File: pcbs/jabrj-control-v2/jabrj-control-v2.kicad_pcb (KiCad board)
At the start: 6 copper layers, 70 x 80 mm, 300 parts, among them J1001 FH12-22S-0.5SH, J1002 FH12-22S-0.5SH, J301 43045-0201, J401 MDT420E0X001, J701 FFC3A20-05-G, J702 JST-SH-4-Vertical, J801 MSPE-J2L0-x00, J901 48406-0003, J902 ARJM11D7-502-AB-EW2, J903 TYPE-C-31-M-12, Q401 DMN21D2UFB-7B, Q402 DMN21D2UFB-7B, Q403 DMN21D2UFB-7B, Q701 DMN21D2UFB-7B, SW701 TS20-42-25-WT-160-SMT-TR, U301 SYA75603A, U302 TVS3301DRBR, U303 PCI11010C, U304 TPS26600RHFR, U305 AT24C64D-MAHM-E, U401 AZV3001FZ4-7, U402 TPS259472ARPWR, U403 MAX20008AFOC/VY+T, U501 TPS7B8133QDRVRQ1, U502 TPS2116DRL, U601 TPS22991CNRAAR, U602 TPS62827DMQR, U603 TPS62825DMQR, U701 PESD4USB3BTTS-QX, U702 NX3DV221GM, U801 LAN8870, U901 PESD4USB3BTTS-QX, U902 PESD4USB3BTTS-QX, U903 PESD4USB3BTTS-QX, U904 PESD4USB3BTTS-QX, U905 PESD4USB3BTTS-QX, U906 AP22653FDZ-7, U907 PESD4USB3BTTS-QX, Y301 XRCGB25M000F3A16R0, Y401 ASEK-32.768KHZ-LRT, Y801 XRCGB25M000F3A16R0

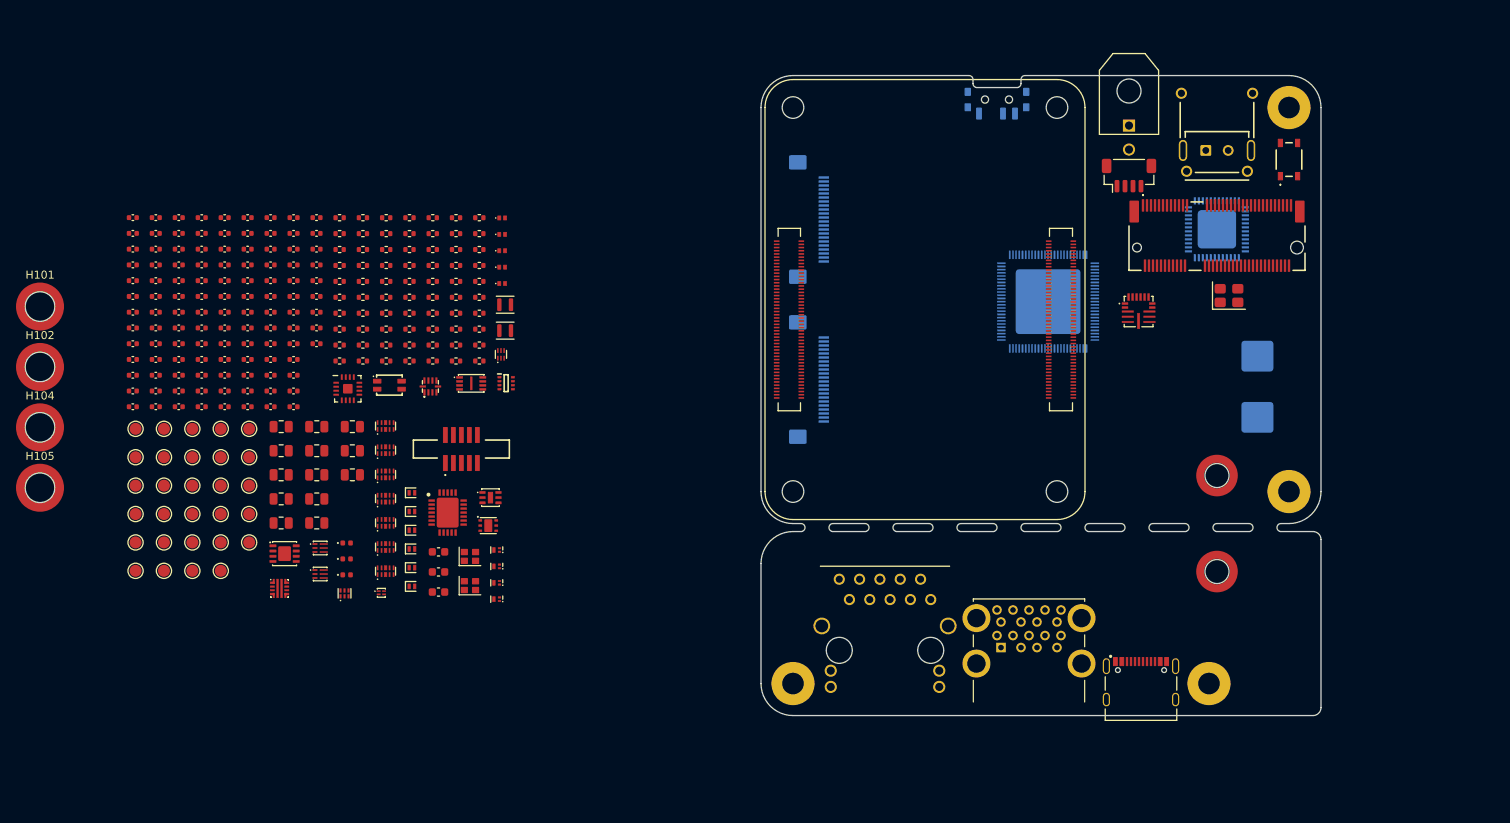
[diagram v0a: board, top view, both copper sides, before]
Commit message: Fixed 5V buck inductor value
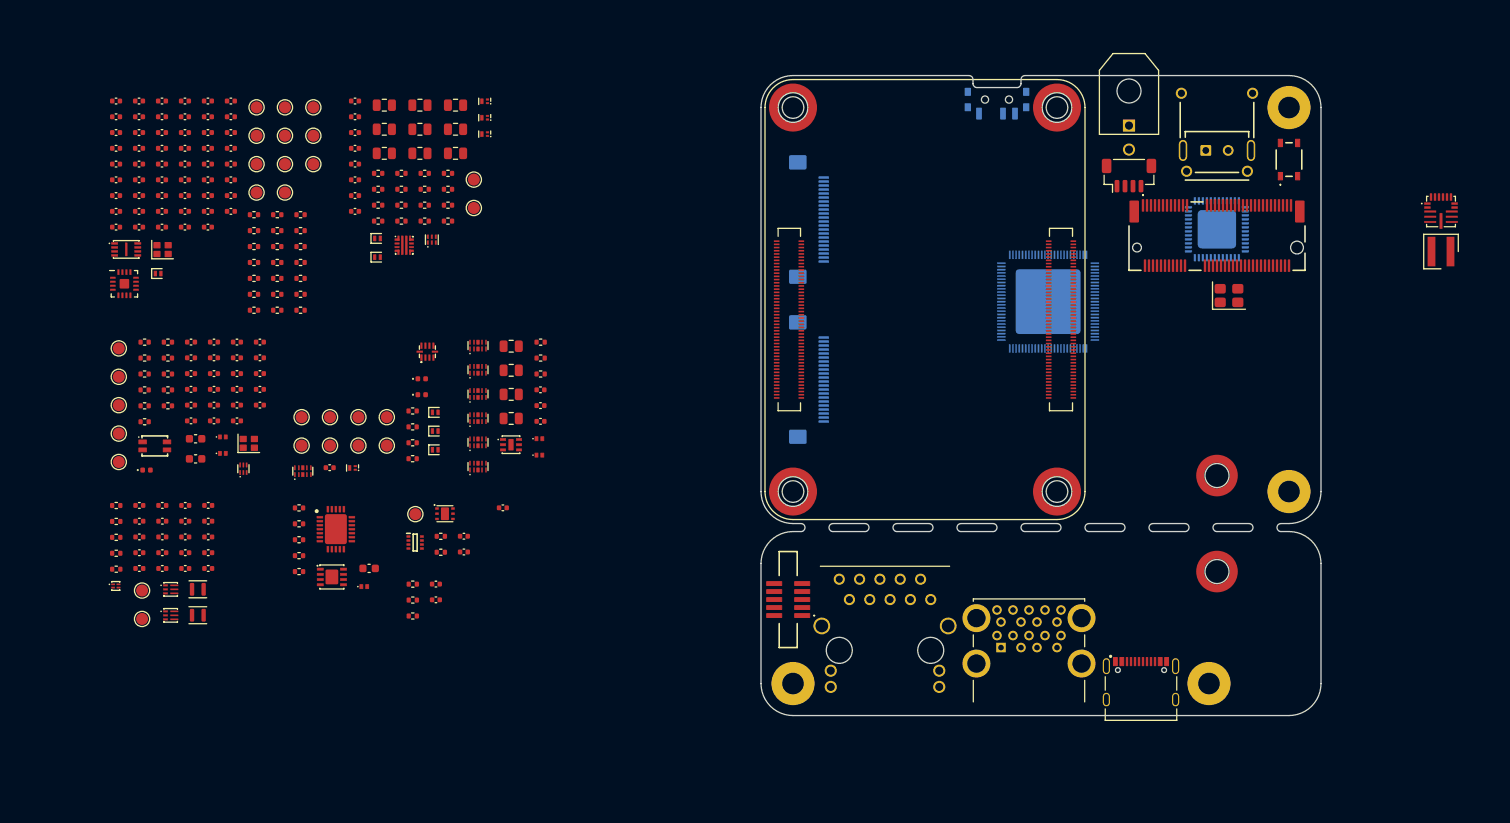
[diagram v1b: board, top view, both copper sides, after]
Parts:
- removed C302, C303, C304, C305, C306, C307, C312, C313, C314, C319, C320, C321, C326, C327, C328, C330, C331, C335, C337, C338, C339, C341, C343, C345, C347, C352: 1n, project_footprints:C_0402
- removed C308, C309, C322, C323, C332, C333, C336, C340, C342, C344, C346, C348, C349, C351, C810, C811, C812, C813, C814, C815, C818, C819, C820: 100n, project_footprints:C_0402
- removed C310, C311, C324, C325, C334, C808, C817: 1u, project_footprints:C_0402
- removed C315, C316, C317, C318: 220n, project_footprints:C_0402
- removed C329, C824, C825: 100n, project_footprints:C_0603
- removed C350, C809, C816, C823, C906, C907: 4u7, project_footprints:C_0402
- removed C353, C354, C821, C822: 10p, project_footprints:C_0402
- removed C418, C903, C904, C905: 22u, project_footprints:C_0805
- removed D302, D803, D804: SZESD7241N2T5G, project_footprints:SZESD7462N2T5G
- removed D901, D902: SZESD8472MUT5G, project_footprints:SZESD7462N2T5G
- removed FL801: ACT1210G-800-2P-TL10, project_footprints:ACT1210G
- removed L401: 784325078, project_footprints:784325078
- removed R306, R315, R319, R325, R326, R810: 1k, project_footprints:R_0402
- removed R307, R312, R322: 100k, project_footprints:R_0402
- removed R308: 120k, project_footprints:R_0402
- removed R309, R311, R314, R316, R317, R320, R321, R324, R804, R805, R807, R808, R809, R811: 10k, project_footprints:R_0402
- removed R310: 4k7, project_footprints:R_0402
- removed R313: 2k2, project_footprints:R_0402
- removed R318: 22k, project_footprints:R_0402
- removed R323: 200R, project_footprints:R_0402
- removed R806: 12k1, project_footprints:R_0402
- removed TP301, TP302, TP303, TP304, TP305, TP306, TP307, TP308, TP309, TP310, TP311, TP801, TP802, TP803, TP804, TP805: 1.5mm, project_footprints:TestPoint_Pad_D1.5mm
- removed U304: TPS26600RHFR, project_footprints:QFN50P400X500X100-25N-D
- removed U305: AT24C64D-MAHM-E, project_footprints:SON50P300X200X60-9N
- removed U901, U902, U903, U904, U905, U907: PESD4USB3BTTS-QX, project_footprints:PESD4USB3BTTSQX
- removed U906: AP22653FDZ-7, project_footprints:SON65P200X200X80-7N-D
- removed Y301, Y801: XRCGB25M000F3A16R0, project_footprints:XRCGB25M000F3A16R0
- added C1003: 1n, project_footprints:C_0402, F.Cu at (48.4, 70.1)
- added C1004: 1n, project_footprints:C_0402, F.Cu at (48.4, 72.1)
- added C1005: 1n, project_footprints:C_0402, F.Cu at (48.4, 74.1)
- added C1006: 1n, project_footprints:C_0402, F.Cu at (48.4, 76.0)
- added C1007: 1n, project_footprints:C_0402, F.Cu at (48.4, 78.0)
- added C1008: 100n, project_footprints:C_0402, F.Cu at (48.4, 80.0)
- added C1009: 100n, project_footprints:C_0402, F.Cu at (48.4, 81.9)
- added C1010: 1u, project_footprints:C_0402, F.Cu at (51.3, 66.2)
- added C1011: 1u, project_footprints:C_0402, F.Cu at (51.3, 68.2)
- added C1012: 1n, project_footprints:C_0402, F.Cu at (51.3, 70.1)
- added C1013: 1n, project_footprints:C_0402, F.Cu at (51.3, 72.1)
- added C1014: 1n, project_footprints:C_0402, F.Cu at (51.3, 74.1)
- added C1015: 220n, project_footprints:C_0402, F.Cu at (51.3, 76.0)
- added C1016: 220n, project_footprints:C_0402, F.Cu at (51.3, 78.0)
- added C1017: 220n, project_footprints:C_0402, F.Cu at (51.3, 80.0)
- added C1018: 220n, project_footprints:C_0402, F.Cu at (51.3, 81.9)
- added C1019: 1n, project_footprints:C_0402, F.Cu at (54.1, 66.2)
- added C1020: 1n, project_footprints:C_0402, F.Cu at (54.1, 68.2)
- added C1021: 1n, project_footprints:C_0402, F.Cu at (54.1, 70.1)
- added C1022: 100n, project_footprints:C_0402, F.Cu at (54.1, 72.1)
- added C1023: 100n, project_footprints:C_0402, F.Cu at (54.1, 74.1)
- added C1024: 1u, project_footprints:C_0402, F.Cu at (54.1, 76.0)
- added C1025: 1u, project_footprints:C_0402, F.Cu at (54.1, 78.0)
- added C1026: 1n, project_footprints:C_0402, F.Cu at (54.1, 80.0)
- added C1027: 1n, project_footprints:C_0402, F.Cu at (54.1, 81.9)
- added C1028: 1n, project_footprints:C_0402, F.Cu at (57.0, 66.2)
- added C1029: 1n, project_footprints:C_0402, F.Cu at (57.0, 68.2)
- added C1030: 1n, project_footprints:C_0402, F.Cu at (57.0, 70.1)
- added C1031: 100n, project_footprints:C_0402, F.Cu at (57.0, 72.1)
- added C1032: 100n, project_footprints:C_0402, F.Cu at (57.0, 74.1)
- added C1033: 1u, project_footprints:C_0402, F.Cu at (57.0, 76.0)
- added C1034: 1n, project_footprints:C_0402, F.Cu at (57.0, 78.0)
- added C1035: 100n, project_footprints:C_0402, F.Cu at (57.0, 80.0)
- added C1036: 1n, project_footprints:C_0402, F.Cu at (57.0, 81.9)
- added C1037: 1n, project_footprints:C_0402, F.Cu at (59.9, 66.2)
- added C1038: 1n, project_footprints:C_0402, F.Cu at (59.9, 68.2)
- added C1039: 100n, project_footprints:C_0402, F.Cu at (59.9, 70.1)
- added C1040: 1n, project_footprints:C_0402, F.Cu at (59.9, 72.1)
- added C1041: 100n, project_footprints:C_0402, F.Cu at (59.9, 74.1)
- added C1042: 1n, project_footprints:C_0402, F.Cu at (59.9, 76.0)
- added C1043: 100n, project_footprints:C_0402, F.Cu at (59.9, 78.0)
- added C1044: 1n, project_footprints:C_0402, F.Cu at (59.9, 80.0)
- added C1045: 100n, project_footprints:C_0402, F.Cu at (59.9, 81.9)
- added C1046: 1n, project_footprints:C_0402, F.Cu at (62.7, 66.2)
- added C1047: 100n, project_footprints:C_0402, F.Cu at (62.7, 68.2)
- added C1048: 100n, project_footprints:C_0402, F.Cu at (62.7, 70.1)
- added C1049: 4u7, project_footprints:C_0402, F.Cu at (62.7, 72.1)
- added C1050: 100n, project_footprints:C_0402, F.Cu at (62.7, 74.1)
- added C1051: 1n, project_footprints:C_0402, F.Cu at (62.7, 76.0)
- added C1052: 10p, project_footprints:C_0402, F.Cu at (62.7, 78.0)
- added C1053: 10p, project_footprints:C_0402, F.Cu at (62.7, 80.0)
- added C1101: 100n, project_footprints:C_0402, F.Cu at (57.8, 96.3)
- added C1102: 100n, project_footprints:C_0402, F.Cu at (57.8, 98.3)
- added C1103: 4u7, project_footprints:C_0402, F.Cu at (57.8, 100.3)
- added C1104: 100n, project_footprints:C_0402, F.Cu at (57.8, 102.2)
- added C1105: 100n, project_footprints:C_0402, F.Cu at (57.8, 104.2)
- added C1106: 100n, project_footprints:C_0402, F.Cu at (57.8, 106.2)
- added C1107: 1u, project_footprints:C_0402, F.Cu at (60.6, 96.3)
- added C1108: 1u, project_footprints:C_0402, F.Cu at (60.6, 98.3)
- added C1109: 4u7, project_footprints:C_0402, F.Cu at (60.6, 100.3)
- added C1110: 100n, project_footprints:C_0402, F.Cu at (60.6, 102.2)
- added C1111: 100n, project_footprints:C_0402, F.Cu at (60.6, 104.2)
- added C1112: 100n, project_footprints:C_0402, F.Cu at (60.6, 106.2)
- added C1113: 100n, project_footprints:C_0402, F.Cu at (63.5, 96.3)
- added C1114: 100n, project_footprints:C_0402, F.Cu at (63.5, 98.3)
- added C1115: 100n, project_footprints:C_0402, F.Cu at (63.5, 100.3)
- added C1116: 4u7, project_footprints:C_0402, F.Cu at (63.5, 102.2)
- added C1117: 1u, project_footprints:C_0402, F.Cu at (63.5, 104.2)
- added C1118: 100n, project_footprints:C_0402, F.Cu at (63.5, 106.2)
- added C1119: 100n, project_footprints:C_0402, F.Cu at (66.4, 96.3)
- added C1120: 100n, project_footprints:C_0402, F.Cu at (66.4, 98.3)
- added C1121: 10p, project_footprints:C_0402, F.Cu at (66.4, 100.3)
- added C1122: 10p, project_footprints:C_0402, F.Cu at (66.4, 102.2)
- added C1123: 4u7, project_footprints:C_0402, F.Cu at (66.4, 104.2)
- added C1124: 100n, project_footprints:C_0603, F.Cu at (58.3, 108.4)
- added C1125: 100n, project_footprints:C_0603, F.Cu at (58.3, 110.9)
- added C1201: 100n, project_footprints:C_0402, F.Cu at (96.7, 117.0)
- added D1001: PMEG4002EL-QYL, project_footprints:PMEG4002EL-QYL, F.Cu at (53.6, 87.8)
- added D1101: GREEN, project_footprints:LED_0402, F.Cu at (52.2, 112.3)
- added D1102: 824012823, project_footprints:824012823, F.Cu at (64.3, 112.2)
- added D1103: SZESD7241N2T5G, project_footprints:SZESD7462N2T5G, F.Cu at (61.7, 108.2)
- added D1104: SZESD7241N2T5G, project_footprints:SZESD7462N2T5G, F.Cu at (61.7, 110.2)
- added FL1101: ACT1210G-800-2P-TL10, project_footprints:ACT1210G, F.Cu at (53.2, 109.3)
- added L402: 7443844020010, project_footprints:L_Wurth_WE-MXGI-4020, F.Cu at (214.0, 85.0)
- added R1004: 1k, project_footprints:R_0402, F.Cu at (65.6, 86.4)
- added R1005: 10k, project_footprints:R_0402, F.Cu at (65.6, 88.4)
- added R1006: 1k, project_footprints:R_0402, F.Cu at (65.6, 90.3)
- added R1007: 100k, project_footprints:R_0402, F.Cu at (65.6, 92.3)
- added R1008: 10k, project_footprints:R_0402, F.Cu at (68.5, 80.4)
- added R1009: 100k, project_footprints:R_0402, F.Cu at (68.5, 82.4)
- added R1010: 2k2, project_footprints:R_0402, F.Cu at (68.5, 84.4)
- added R1011: 1k, project_footprints:R_0402, F.Cu at (68.5, 86.4)
- added R1012: 10k, project_footprints:R_0402, F.Cu at (68.5, 88.4)
- added R1013: 10k, project_footprints:R_0402, F.Cu at (68.5, 90.3)
- added R1014: 1k, project_footprints:R_0402, F.Cu at (68.5, 92.3)
- added R1015: 10k, project_footprints:R_0402, F.Cu at (71.4, 80.4)
- added R1016: 10k, project_footprints:R_0402, F.Cu at (71.4, 82.4)
- added R1017: 100k, project_footprints:R_0402, F.Cu at (71.4, 84.4)
- added R1018: 200R, project_footprints:R_0402, F.Cu at (71.4, 86.4)
- added R1019: 10k, project_footprints:R_0402, F.Cu at (71.4, 88.4)
- added R1020: 1k, project_footprints:R_0402, F.Cu at (71.4, 90.3)
- added R1021: 1k, project_footprints:R_0402, F.Cu at (71.4, 92.3)
- added R1101: 10k, project_footprints:R_0402, F.Cu at (52.0, 96.3)
- added R1102: 10k, project_footprints:R_0402, F.Cu at (52.0, 98.3)
- added R1103: 10k, project_footprints:R_0402, F.Cu at (52.0, 100.3)
- added R1104: 10k, project_footprints:R_0402, F.Cu at (52.0, 102.3)
- added R1105: 10k, project_footprints:R_0402, F.Cu at (52.0, 104.3)
- added R1106: 12k1, project_footprints:R_0402, F.Cu at (52.0, 106.3)
- added R1107: 10k, project_footprints:R_0402, F.Cu at (54.9, 96.3)
- added R1108: 10k, project_footprints:R_0402, F.Cu at (54.9, 98.3)
- added R1109: 10k, project_footprints:R_0402, F.Cu at (54.9, 100.3)
- added R1110: 1k, project_footprints:R_0402, F.Cu at (54.9, 102.3)
- added R1111: 10k, project_footprints:R_0402, F.Cu at (54.9, 104.3)
- added TP1001: 1.5mm, project_footprints:TestPoint_Pad_D1.5mm, F.Cu at (65.9, 67.0)
- added TP1002: 1.5mm, project_footprints:TestPoint_Pad_D1.5mm, F.Cu at (65.9, 70.5)
- added TP1003: 1.5mm, project_footprints:TestPoint_Pad_D1.5mm, F.Cu at (65.9, 74.1)
- added TP1004: 1.5mm, project_footprints:TestPoint_Pad_D1.5mm, F.Cu at (65.9, 77.6)
- added TP1005: 1.5mm, project_footprints:TestPoint_Pad_D1.5mm, F.Cu at (69.5, 67.0)
- added TP1006: 1.5mm, project_footprints:TestPoint_Pad_D1.5mm, F.Cu at (69.5, 70.5)
- added TP1007: 1.5mm, project_footprints:TestPoint_Pad_D1.5mm, F.Cu at (69.5, 74.1)
- added TP1008: 1.5mm, project_footprints:TestPoint_Pad_D1.5mm, F.Cu at (69.5, 77.6)
- added TP1009: 1.5mm, project_footprints:TestPoint_Pad_D1.5mm, F.Cu at (73.0, 67.0)
- added TP1010: 1.5mm, project_footprints:TestPoint_Pad_D1.5mm, F.Cu at (73.0, 70.5)
- added TP1011: 1.5mm, project_footprints:TestPoint_Pad_D1.5mm, F.Cu at (73.0, 74.1)
- added TP1101: 1.5mm, project_footprints:TestPoint_Pad_D1.5mm, F.Cu at (48.7, 97.1)
- added TP1102: 1.5mm, project_footprints:TestPoint_Pad_D1.5mm, F.Cu at (48.7, 100.7)
- added TP1103: 1.5mm, project_footprints:TestPoint_Pad_D1.5mm, F.Cu at (48.7, 104.2)
- added TP1104: 1.5mm, project_footprints:TestPoint_Pad_D1.5mm, F.Cu at (48.7, 107.8)
- added TP1105: 1.5mm, project_footprints:TestPoint_Pad_D1.5mm, F.Cu at (48.7, 111.3)
- added U1001: SYA75603A, project_footprints:SYA7560x, F.Cu at (49.4, 89.0)
- added U1003: AT24C64D-MAHM-E, project_footprints:SON50P300X200X60-9N, F.Cu at (49.6, 84.7)
- added U801: PESD4USB3BTTS-QX, project_footprints:PESD4USB3BTTSQX, F.Cu at (93.6, 96.8)
- added U802: PESD4USB3BTTS-QX, project_footprints:PESD4USB3BTTSQX, F.Cu at (93.6, 99.8)
- added U803: PESD4USB3BTTS-QX, project_footprints:PESD4USB3BTTSQX, F.Cu at (93.6, 102.8)
- added U804: PESD4USB3BTTS-QX, project_footprints:PESD4USB3BTTSQX, F.Cu at (93.6, 105.8)
- added U805: PESD4USB3BTTS-QX, project_footprints:PESD4USB3BTTSQX, F.Cu at (93.6, 108.9)
- added U806: AP22653FDZ-7, project_footprints:SON65P200X200X80-7N-D, F.Cu at (97.8, 109.1)
- added U807: PESD4USB3BTTS-QX, project_footprints:PESD4USB3BTTSQX, F.Cu at (93.6, 111.9)
- added Y1001: XRCGB25M000F3A16R0, project_footprints:XRCGB25M000F3A16R0, F.Cu at (54.2, 84.8)
- added Y1101: XRCGB25M000F3A16R0, project_footprints:XRCGB25M000F3A16R0, F.Cu at (65.0, 109.0)
- C1001, C1002: value 4u7 -> 1n
- C301: value 1n -> 100n; footprint project_footprints:C_0402 -> project_footprints:C_0603
- C414, C802, C804, C805: value 100n -> 22u; footprint project_footprints:C_0402 -> project_footprints:C_0805
- C803: value 4u7 -> 22u; footprint project_footprints:C_0402 -> project_footprints:C_0805
- C806, C901: value 100n -> 4u7
- C807: value 1u -> 4u7
- C902: value 22u -> 4u7; footprint project_footprints:C_0805 -> project_footprints:C_0402
- D301: value PMEG4002EL-QYL -> SZESD7241N2T5G; footprint project_footprints:PMEG4002EL-QYL -> project_footprints:SZESD7462N2T5G
- D801: value GREEN -> SZESD8472MUT5G; footprint project_footprints:LED_0402 -> project_footprints:SZESD7462N2T5G
- D802: value 824012823 -> SZESD8472MUT5G; footprint project_footprints:824012823 -> project_footprints:SZESD7462N2T5G
- R1001, R1002, R1003: value 2k2 -> 10k
- R301: value 10k -> 120k
- R303: value 10k -> 4k7
- R304: value 1k -> 10k
- R305: value 10k -> 22k
- R801, R802: value 10k -> 470R
- R803: value 10k -> 12k1
- R901, R902: value 470R -> 2k2
- R903: value 12k1 -> 2k2
- U301: value SYA75603A -> TVS3301DRBR; footprint project_footprints:SYA7560x -> project_footprints:SON65P300X300X100-9N-D
- U302: value TVS3301DRBR -> TPS26600RHFR; footprint project_footprints:SON65P300X300X100-9N-D -> project_footprints:QFN50P400X500X100-25N-D
- moved H104 133.3 mm to (166.0, 67.0)
- moved H105 127.1 mm to (166.0, 115.0)
- moved H101 97.4 mm to (133.0, 67.0)
- moved H102 95.4 mm to (133.0, 115.0)
- moved Q401 58.2 mm to (94.5, 66.2)
- moved Q403 58.2 mm to (94.5, 70.3)
- moved Q402 58.2 mm to (94.5, 68.3)
- moved R602 56.7 mm to (48.4, 118.7)
- moved R603 56.7 mm to (48.4, 120.7)
- moved R604 56.7 mm to (48.4, 122.7)
- moved R605 56.7 mm to (48.4, 124.7)
- moved C415 55.0 mm to (90.8, 66.7)
- moved C402 53.8 mm to (81.9, 66.7)
- moved L601 52.4 mm to (58.6, 127.2)
- moved L602 52.4 mm to (58.6, 130.5)
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- renumbered H401 to H1201, H402 to H1202, J801 to J1101, J401 to J1201, J901 to J801, J902 to J802, J903 to J803, J1001 to J901, J1002 to J902, U303 to U1002, U801 to U1101, Y401 to Y1201
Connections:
- C1001 pad 1: +3V3 -> +1V1
- C1002 pad 1: +3V3 -> +3V3_PCIE
- C301 pad 1: +1V1 -> GND
- C301 pad 2: GND -> /Power/Power In/VIN_RAW
- C414 pad 1: +3V3_PCIE -> +5V
- C801 pad 1: +3V3_PCIE -> /CM5IO/CT
- C802 pad 1: +3V3_PCIE -> /CM5IO/VBUS_OUT
- C803 pad 1: +3V3_PCIE -> /CM5IO/VBUS_OUT
- C804 pad 1: +3V3_PCIE -> /CM5IO/VBUS_OUT
- C805 pad 1: +3V3_PCIE -> /CM5IO/VBUS_OUT
- C806 pad 1: +3V3_AON -> +5V
- C807 pad 1: +3V3_PCIE -> +5V
- C901 pad 1: /CM5IO/CT -> +3V3
- C902 pad 1: /CM5IO/VBUS_OUT -> +3V3
- D301 pad 1: /PCIe Switch/~{PORT1_CLKREQ} -> GND
- D301 pad 2: /PCIe Switch/~{OE0} -> /Power/Power In/VIN_RAW
- D801 pad 1: /1000BASE-T1 PHY/LINK_LED -> GND
- D801 pad 2: +1V8_PCIE -> /CM5IO/VBUS_OUT
- D802 pad 1: /1000BASE-T1 PHY/TRXN -> VBUS
- D802 pad 2: /1000BASE-T1 PHY/TRXP -> GND
- R1001 pad 1: /MIPI Connectors/~{MIPI1_RST} -> +3V3_PCIE
- R1001 pad 2: +3V3 -> /PCIe Switch/~{PORT1_CLKREQ}
- R1002 pad 1: /CM5/MIPI1.SCL -> +1V8_PCIE
- R1002 pad 2: +3V3 -> /PCIe Switch/~{OE0}
- R1003 pad 1: /CM5/MIPI1.SDA -> +3V3_PCIE
- R1003 pad 2: +3V3 -> /M.2 E-Key/M2_I2C.~{INT}
- R301 pad 1: +3V3_PCIE -> /Power/Power In/VIN_RAW
- R301 pad 2: /PCIe Switch/~{PORT1_CLKREQ} -> /Power/Power In/UVLO
- R302 pad 1: +1V8_PCIE -> /Power/Power In/UVLO
- R302 pad 2: /PCIe Switch/~{OE0} -> /Power/Power In/OVP
- R303 pad 1: +3V3_PCIE -> /Power/Power In/OVP
- R303 pad 2: /M.2 E-Key/M2_I2C.~{INT} -> /Power/Power In/RTN
- R304 pad 1: +3V3_PCIE -> /Power/Power In/RTN
- R304 pad 2: /M.2 E-Key/M2_I2C.SCL -> /Power/Power In/ILIM
- R305 pad 1: /PCIe Switch/VAUX_DET -> /Power/Power In/RTN
- R305 pad 2: GND -> /Power/Power In/ILIM
- R801 pad 1: +1V8_PCIE -> /CM5IO/LEDG
- R801 pad 2: /1000BASE-T1 PHY/RX_D0 -> /CM5/ETH_LED2
- R802 pad 1: /1000BASE-T1 PHY/RX_D1 -> /CM5IO/LEDY
- R802 pad 2: GND -> /CM5/ETH_LED3
- R803 pad 1: /1000BASE-T1 PHY/RX_D2 -> /CM5IO/ILIM
- R901 pad 1: /CM5IO/LEDG -> /MIPI Connectors/~{MIPI1_RST}
- R901 pad 2: /CM5/ETH_LED2 -> +3V3
- R902 pad 1: /CM5IO/LEDY -> /CM5/MIPI1.SCL
- R902 pad 2: /CM5/ETH_LED3 -> +3V3
- R903 pad 1: /CM5IO/ILIM -> /CM5/MIPI1.SDA
- R903 pad 2: GND -> +3V3
- U301 pad 1: /CM5/CLK_P -> /Power/Power In/VIN_RAW
- U301 pad 2: /CM5/CLK_N -> /Power/Power In/VIN_RAW
- U301 pad 3: unconnected-(U301-NC-Pad3) -> /Power/Power In/VIN_RAW
- U301 pad 4: unconnected-(U301-NC-Pad4) -> /Power/Power In/VIN_RAW
- U301 pad 5: unconnected-(U301-NC-Pad5) -> GND
- U301 pad 6: unconnected-(U301-NC-Pad6) -> GND
- U301 pad 7: unconnected-(U301-NC-Pad7) -> GND
- U301 pad 8: unconnected-(U301-NC-Pad8) -> GND
- U301 pad 9: GND -> unconnected-(U301-NC-Pad9)
- U302 pad 1: /Power/Power In/VIN_RAW -> unconnected-(U302-NC-Pad1)
- U302 pad 2: /Power/Power In/VIN_RAW -> unconnected-(U302-NC-Pad2)
- U302 pad 3: /Power/Power In/VIN_RAW -> unconnected-(U302-NC-Pad3)
- U302 pad 4: /Power/Power In/VIN_RAW -> unconnected-(U302-NC-Pad4)
- U302 pad 5: GND -> unconnected-(U302-NC-Pad5)
- U302 pad 6: GND -> unconnected-(U302-NC-Pad6)
- U302 pad 7: GND -> unconnected-(U302-NC-Pad7)
- U302 pad 8: GND -> /Power/Power In/VIN_RAW
- U302 pad 9: unconnected-(U302-NC-Pad9) -> /Power/Power In/VIN_RAW
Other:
- outline, holes or cut-outs redrawn

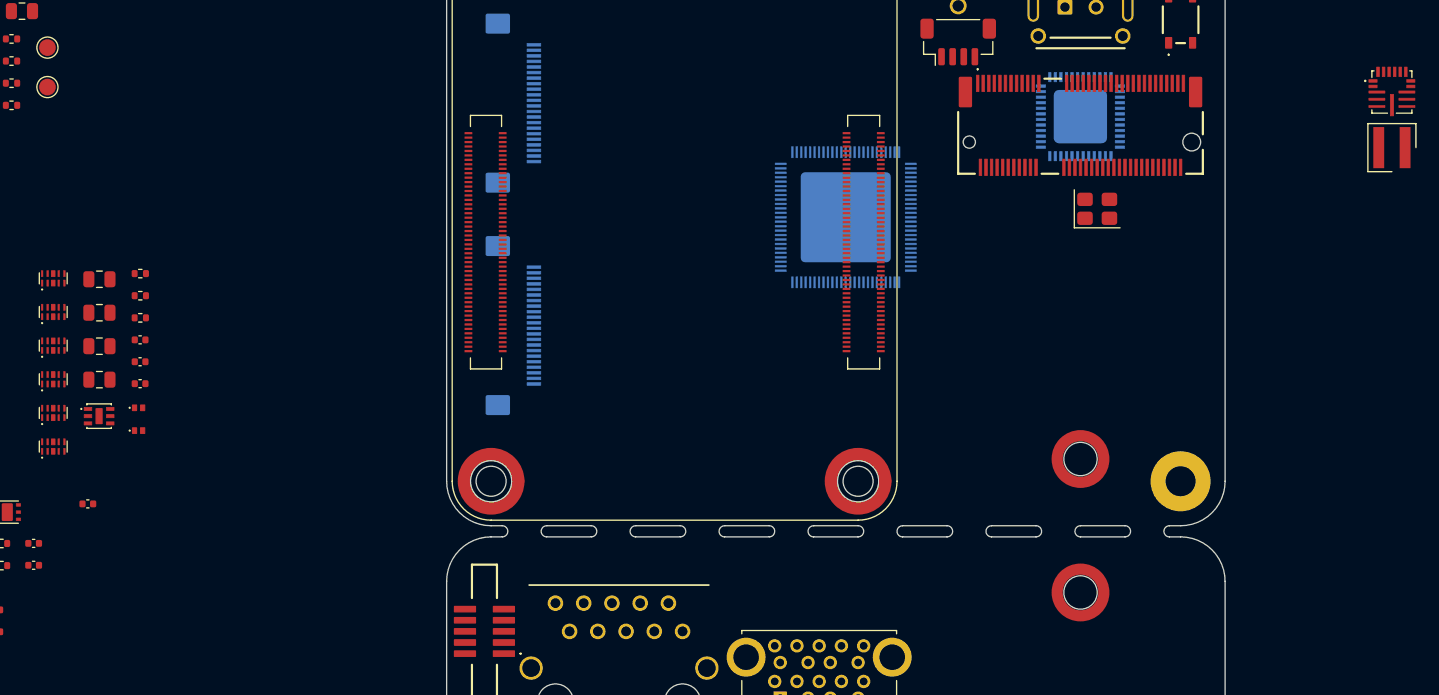
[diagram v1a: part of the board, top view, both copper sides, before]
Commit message: Minor schematic fixes
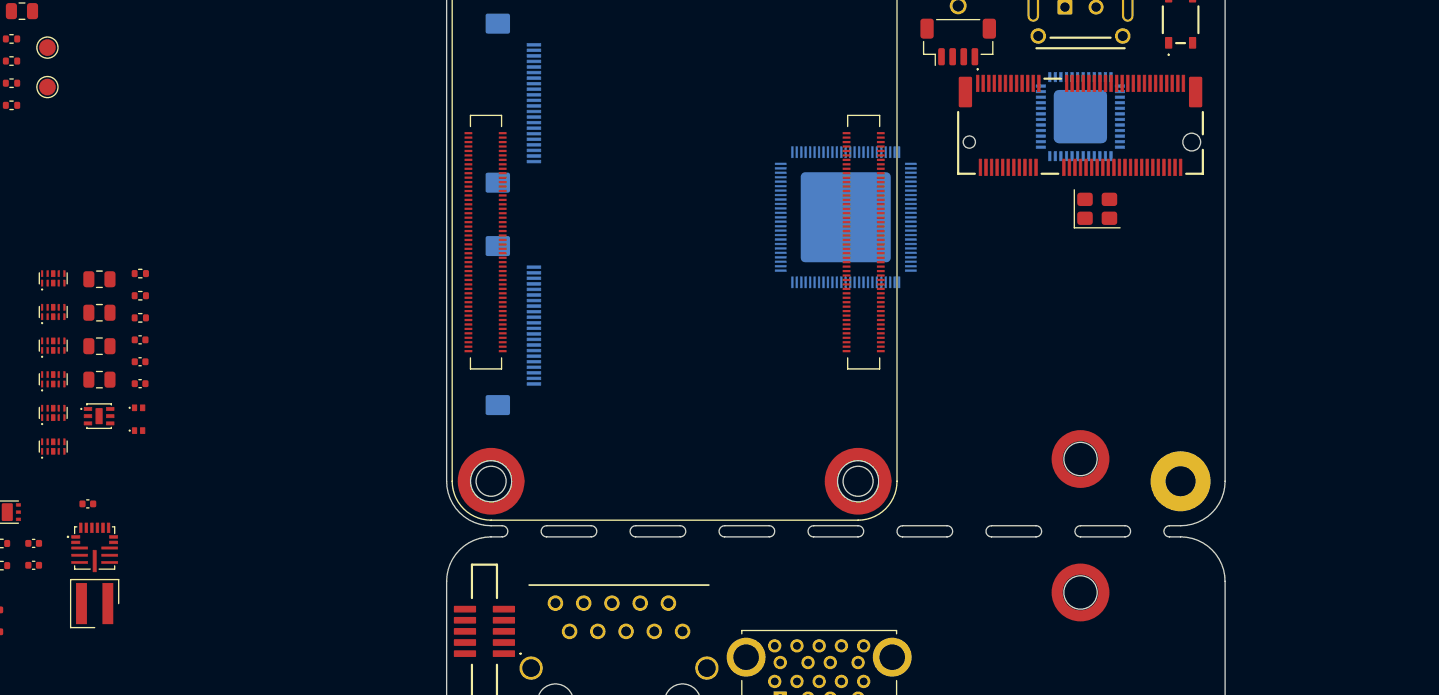
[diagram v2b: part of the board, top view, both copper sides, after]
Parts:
- moved L402 123.6 mm to (97.3, 126.0)
- moved U403 123.6 mm to (97.3, 121.0)
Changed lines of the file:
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@@
 	(footprint "project_footprints:L_Wurth_WE-MXGI-4020"
 		(layer "F.Cu")
-		(at 214 85 180)
+		(at 97.35 126 180)
 		(descr "Shielded Power Inductor, body 4.1x4.1x2.1mm, https://www.we-online.com/en/components/products/WE-MXGI#/articles/WE-MXGI_SIZE_4020")
 		(tags "SMT")
@@
 			(polygon
 				(pts
-					(xy 214.695 82.7) (xy 213.305 82.7) (xy 213.305 87.3) (xy 214.695 87.3)
+					(xy 98.045 123.7) (xy 96.655 123.7) (xy 96.655 128.3) (xy 98.045 128.3)
 				)
 			)
@@
 	(footprint "project_footprints:MAX20004AFOC_VY+"
 		(layer "F.Cu")
-		(at 214 80)
+		(at 97.35 121)
 		(descr "MAX20004AFOA/VY+T-2")
 		(tags "Integrated Circuit")

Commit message: Layout started
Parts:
- removed TP1005, TP1006, TP1101: 1.5mm, project_footprints:TestPoint_Pad_D1.5mm
- added J804: FH12-20S-0.5SH, project_footprints:Hirose_FH12-20S-0.5SH_1x20-1MP_P0.50mm_Horizontal, B.Cu at (177.0, 113.5)
- added J805: FH12-20S-0.5SH, project_footprints:Hirose_FH12-20S-0.5SH_1x20-1MP_P0.50mm_Horizontal, B.Cu at (146.5, 113.5)
- added R1011: 22R, project_footprints:R_0402, F.Cu at (68.5, 144.0)
- added R1012: 22R, project_footprints:R_0402, F.Cu at (68.5, 146.0)
- added R1013: 22R, project_footprints:R_0402, F.Cu at (68.5, 148.0)
- added R1014: 22R, project_footprints:R_0402, F.Cu at (68.5, 150.0)
- added R1015: 22R, project_footprints:R_0402, F.Cu at (68.5, 152.0)
- added R1016: 22R, project_footprints:R_0402, F.Cu at (68.5, 153.9)
- added R1107: 22R, project_footprints:R_0402, F.Cu at (76.9, 144.0)
- added R1108: 22R, project_footprints:R_0402, F.Cu at (76.9, 146.0)
- added R1109: 22R, project_footprints:R_0402, F.Cu at (76.9, 148.0)
- added R1110: 22R, project_footprints:R_0402, F.Cu at (76.9, 150.0)
- added R1111: 22R, project_footprints:R_0402, F.Cu at (76.9, 152.0)
- added R1112: 22R, project_footprints:R_0402, F.Cu at (76.9, 153.9)
- added TP101: 1.5mm, project_footprints:TestPoint_Pad_D1.5mm, F.Cu at (85.7, 144.8)
- added TP102: 1.5mm, project_footprints:TestPoint_Pad_D1.5mm, F.Cu at (85.7, 148.3)
- added TP103: 1.5mm, project_footprints:TestPoint_Pad_D1.5mm, F.Cu at (85.7, 151.9)
- added TP1106: 1.5mm, project_footprints:TestPoint_Pad_D1.5mm, F.Cu at (80.1, 144.8)
- C1015, C1016, C1017, C1018, C1048, C1049, C1050, C1052, C1053, C1121, C1122, C1124, C1125, C1201, C301, C402, C403, C404, C405, C410, C411, C412, C413, C414, C415, C416, C417, C501, C502, C601, C602, C603, C604, C605, C606, C607, C608, C609, C610, C611, C612, C613, C614, C615, C616, C617, C618, C619, C620, D1102, D1103, D1104, D301, D401, D402, FL1101, L601, L602, R301, R302, R303, R304, R305, R402, R403, R404, R405, R406, R410, R411, R601, R602, R603, R604, R605, TP1008, TP1009, TP1010, TP1011, TP401, TP501, TP601, TP602, U1003, U301, U302, U401, U403, U501, U502, U601, U602, U603, U701, U801, U802, U803, U804, U805, Y1001, Y1101, Y1201: moved to B.Cu
- C406: footprint project_footprints:C_0805 -> project_footprints:C_0603; moved to B.Cu
- C407: footprint project_footprints:C_0402 -> project_footprints:C_0603; moved to B.Cu
- L401: renamed from L402; moved to B.Cu
- R1026: renamed from R1020; moved to B.Cu
- R1027: renamed from R1021; moved to B.Cu
- R401: value 10k -> 100k; moved to B.Cu
- R501: value 47k -> 100k; moved to B.Cu
- R502: value 22k -> 56k; moved to B.Cu
- moved U601 172.1 mm to (218.8, 102.8), turned to 90 degrees
- moved C605 170.4 mm to (220.3, 102.8), turned to 90 degrees
- moved R601 166.8 mm to (214.1, 135.7), turned to 90 degrees
- moved C606 163.7 mm to (217.3, 102.8), turned to -90 degrees
- moved R603 138.7 mm to (185.0, 96.5), turned to 180 degrees
- moved R602 138.1 mm to (185.0, 98.5)
- moved R605 138.0 mm to (185.0, 105.0), turned to 180 degrees
- moved C603 137.2 mm to (185.5, 92.0), turned to 90 degrees
- moved C604 136.0 mm to (185.5, 100.5), turned to 90 degrees
- moved FL1101 135.8 mm to (186.0, 80.8), turned to -90 degrees
- moved R604 135.6 mm to (183.0, 106.0)
- moved C601 135.5 mm to (184.5, 92.0), turned to 90 degrees
- moved TP602 134.6 mm to (180.5, 92.0), turned to 90 degrees
- moved C602 134.4 mm to (184.5, 100.5), turned to 90 degrees
- moved R405 133.3 mm to (209.0, 121.7)
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- renumbered R1012 to R1017, R1013 to R1018, R1016 to R1019, R1015 to R1020, R1011 to R1021, R1014 to R1022, R1017 to R1023, R1018 to R1024, R1019 to R1025, R1105 to R1104, R1107 to R1105, R1104 to R1106, R1106 to R1113, R1108 to R1114, R1109 to R1115, R1110 to R1116, R1111 to R1117
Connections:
- net /CM5/VBUS_EN renamed /CM5IO/VBUS_EN
- J701 pad 1: +5V -> +3V3
- R1106 pad 1: /1000BASE-T1 PHY/MODE -> /1000BASE-T1 PHY/PPS
- R1114 pad 2: /1000BASE-T1 PHY/~{INT} -> /1000BASE-T1 PHY/SPEED_SEL
- R1115 pad 2: /1000BASE-T1 PHY/SPEED_SEL -> /1000BASE-T1 PHY/~{INT}
- U1002 pad 31: /PCIe Switch/PTP_IO0 -> /1000BASE-T1 PHY/PPS
- U1002 pad 53: /1000BASE-T1 PHY/TX_CLK -> /PCIe Switch/TX_CLK_R
- U1002 pad 54: /1000BASE-T1 PHY/TX_CTL -> /PCIe Switch/TX_CT_R
- U1002 pad 56: /1000BASE-T1 PHY/TX_D0 -> /PCIe Switch/TX_D0_R
- U1002 pad 57: /1000BASE-T1 PHY/TX_D1 -> /PCIe Switch/TX_D1_R
- U1002 pad 58: /1000BASE-T1 PHY/TX_D2 -> /PCIe Switch/TX_D2_R
- U1002 pad 59: /1000BASE-T1 PHY/TX_D3 -> /PCIe Switch/TX_D3_R
- U1101 pad 11: /1000BASE-T1 PHY/RX_D0 -> /1000BASE-T1 PHY/RX_D0_R
- U1101 pad 12: /1000BASE-T1 PHY/RX_D1 -> /1000BASE-T1 PHY/RX_D1_R
- U1101 pad 14: /1000BASE-T1 PHY/RX_D2 -> /1000BASE-T1 PHY/RX_D2_R
- U1101 pad 15: /1000BASE-T1 PHY/RX_D3 -> /1000BASE-T1 PHY/RX_D3_R
- U1101 pad 16: /1000BASE-T1 PHY/RX_CLK -> /1000BASE-T1 PHY/RX_CLK_R
- U1101 pad 17: /1000BASE-T1 PHY/RX_CTL -> /1000BASE-T1 PHY/RX_CTL_R
- U1101 pad 18: /1000BASE-T1 PHY/MODE -> /1000BASE-T1 PHY/PPS
- U802 pad 1: /CM5/USB3_0.DP -> /CM5/USB3_1.RX_P
- U802 pad 10: /CM5/USB3_0.DP -> /CM5/USB3_1.RX_P
- U802 pad 2: /CM5/USB3_0.DN -> /CM5/USB3_1.RX_N
- U802 pad 9: /CM5/USB3_0.DN -> /CM5/USB3_1.RX_N
- U805 pad 1: /CM5/USB3_1.RX_P -> /CM5/USB3_0.DP
- U805 pad 10: /CM5/USB3_1.RX_P -> /CM5/USB3_0.DP
- U805 pad 2: /CM5/USB3_1.RX_N -> /CM5/USB3_0.DN
- U805 pad 9: /CM5/USB3_1.RX_N -> /CM5/USB3_0.DN
